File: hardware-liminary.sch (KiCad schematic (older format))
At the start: 51 parts, among them IC1 MCP6001T-I_OT, J1 Conn_01x05, J2 Conn_01x03, J3 Conn_01x03, J4 SWD, J5 Console, J6 UFL-Conn, K1 HL2-1CH-12S, Q1 CMBT3904, Q2 PT204-6C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

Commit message: relay
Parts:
- removed K1: HL2-1CH-12S, symbol Relay:DIPxx-1Cxx-51x
- added K?: HL2-1CH-12S, Relay_THT:HL2-1CH-12S, symbol proyect_new:HL2-1CH-12S
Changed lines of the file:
@@
 	850  3200 1050 3200
-$Comp
-L Relay:DIPxx-1Cxx-51x K1
-U 1 1 5F8071A4
-P 6200 7700
-F 0 "K1" V 6767 7700 50  0000 C CNN
-F 1 "HL2-1CH-12S" V 6676 7700 50  0000 C CNN
-F 2 "" H 6650 7650 50  0001 L CNN
-F 3 "https://standexelectronics.com/wp-content/uploads/datasheet_reed_relay_DIP.pdf" H 6200 7700 50  0001 C CNN
-	1    6200 7700
-	0    -1   -1   0
-$EndComp
 $Comp
 L Diode:1N4007 D1
@@
 Wire Wire Line
 	2600 1350 3000 1350
+$Comp
+L proyect_new:HL2-1CH-12S K?
+U 1 1 5F7D0ED4
+P 6200 7700
+F 0 "K?" V 6767 7700 50  0000 C CNN
+F 1 "HL2-1CH-12S" V 6676 7700 50  0000 C CNN
+F 2 "Relay_THT:HL2-1CH-12S" H 6650 7650 50  0001 L CNN
+F 3 "https://standexelectronics.com/wp-content/uploads/datasheet_reed_relay_DIP.pdf" H 6200 7700 50  0001 C CNN
+	1    6200 7700
+	0    -1   -1   0
+$EndComp
 $EndSCHEMATC

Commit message: Todas las footprint asignadas
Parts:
- removed L2: L_Core_Iron, symbol Device:L_Core_Iron
- added L2: L_Core_Ferrite, Inductor_SMD:L_0805_2012Metric_Pad1.15x1.40mm_HandSolder, symbol Device:L_Core_Ferrite
- JP2: footprint (none) -> Jumper:SolderJumper-2_P1.3mm_Open_TrianglePad1.0x1.5mm
- L1: footprint (none) -> Inductor_SMD:L_Taiyo-Yuden_MD-2020
- Q1, Q3, U2: footprint (none) -> Package_TO_SOT_SMD:SOT-23_Handsoldering
- SW1: footprint (none) -> Button_Switch_SMD:SW_Push_1P1T_NO_6x6mm_H9.5mm
- gave numbers to parts that had none: 1
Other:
- note added: "Program & Console"
- note removed: "Program & Debug"
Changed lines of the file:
@@
 F 0 "L1" V 7240 900 50  0000 C CNN
 F 1 "3.3uH" V 7149 900 50  0000 C CNN
-F 2 "" H 7050 900 50  0001 C CNN
+F 2 "Inductor_SMD:L_Taiyo-Yuden_MD-2020" H 7050 900 50  0001 C CNN
 F 3 "~" H 7050 900 50  0001 C CNN
 	1    7050 900
-	0    -1   -1   0
-$EndComp
-$Comp
-L Device:L_Core_Iron L2
-U 1 1 5F74052A
-P 6350 1950
-F 0 "L2" V 6575 1950 50  0000 C CNN
-F 1 "L_Core_Iron" V 6484 1950 50  0000 C CNN
-F 2 "" H 6350 1950 50  0001 C CNN
-F 3 "~" H 6350 1950 50  0001 C CNN
-	1    6350 1950
 	0    -1   -1   0
 $EndComp
@@
 F 0 "U2" H 5700 1142 50  0000 C CNN
 F 1 "LD1117S33TR_SOT223" H 5700 1051 50  0000 C CNN
-F 2 "" H 5700 1100 50  0001 C CNN
+F 2 "Package_TO_SOT_SMD:SOT-23_Handsoldering" H 5700 1100 50  0001 C CNN
 F 3 "http://www.st.com/st-web-ui/static/active/en/resource/technical/document/datasheet/CD00000544.pdf" H 5800 650 50  0001 C CNN
 	1    5700 900
@@
 F 0 "Q3" H 1791 4096 50  0000 L CNN
 F 1 "CMBT2222A" H 1791 4005 50  0000 L CNN
-F 2 "" H 1800 4150 50  0001 C CNN
+F 2 "Package_TO_SOT_SMD:SOT-23_Handsoldering" H 1800 4150 50  0001 C CNN
 F 3 "~" H 1600 4050 50  0001 C CNN
 	1    1600 4050
@@
 F 0 "Q1" H 6841 8546 50  0000 L CNN
 F 1 "CMBT3904" H 6841 8455 50  0000 L CNN
-F 2 "" H 6850 8600 50  0001 C CNN
+F 2 "Package_TO_SOT_SMD:SOT-23_Handsoldering" H 6850 8600 50  0001 C CNN
 F 3 "~" H 6650 8500 50  0001 C CNN
 	1    6650 8500
@@
 F 0 "JP2" H 7000 7735 50  0000 C CNN
 F 1 "Jumper_2_Open" H 7000 7644 50  0000 C CNN
-F 2 "" H 7000 7500 50  0001 C CNN
+F 2 "Jumper:SolderJumper-2_P1.3mm_Open_TrianglePad1.0x1.5mm" H 7000 7500 50  0001 C CNN
 F 3 "~" H 7000 7500 50  0001 C CNN
 	1    7000 7500
@@
 F 0 "SW1" H 4600 6535 50  0000 C CNN
 F 1 "SW_Push" H 4600 6444 50  0000 C CNN
-F 2 "" H 4600 6450 50  0001 C CNN
+F 2 "Button_Switch_SMD:SW_Push_1P1T_NO_6x6mm_H9.5mm" H 4600 6450 50  0001 C CNN
 F 3 "~" H 4600 6450 50  0001 C CNN
 	1    4600 6250
@@
 $EndComp
 Text Notes 1000 9150 0    118  ~ 24
-Program & Debug
-Wire Notes Line
-	950  8950 950  10700
-Wire Notes Line
-	950  10700 2650 10700
-Wire Notes Line
-	2650 10700 2650 8950
-Wire Notes Line
-	2650 8950 950  8950
+Program & Console
 Text Notes 5250 7050 0    118  ~ 24
 Relay Module
@@
 $EndComp
 $Comp
-L power:GNDA #PWR0114
-U 1 1 5F89AEDC
-P 9050 9950
-F 0 "#PWR0114" H 9050 9700 50  0001 C CNN
-F 1 "GNDA" H 9055 9777 50  0000 C CNN
-F 2 "" H 9050 9950 50  0001 C CNN
-F 3 "" H 9050 9950 50  0001 C CNN
-	1    9050 9950
-	1    0    0    -1
-$EndComp
-$Comp
-L power:PWR_FLAG #FLG0101
-U 1 1 5F89C39F
-P 9050 9950
-F 0 "#FLG0101" H 9050 10025 50  0001 C CNN
-F 1 "PWR_FLAG" H 9050 10123 50  0000 C CNN
-F 2 "" H 9050 9950 50  0001 C CNN
-F 3 "~" H 9050 9950 50  0001 C CNN
-	1    9050 9950
-	1    0    0    -1
-$EndComp
-$Comp
 L proyect_12-22_LEDs:12-22SURSYGC_S530-A2_TR8 LED1
 U 1 1 5F8A983B
@@
 	2600 1350 3000 1350
 $Comp
-L proyect_new:HL2-1CH-12S K?
+L proyect_new:HL2-1CH-12S K1
 U 1 1 5F7D0ED4
 P 6200 7700
-F 0 "K?" V 6767 7700 50  0000 C CNN
+F 0 "K1" V 6767 7700 50  0000 C CNN
 F 1 "HL2-1CH-12S" V 6676 7700 50  0000 C CNN
 F 2 "Relay_THT:HL2-1CH-12S" H 6650 7650 50  0001 L CNN
@@
 	0    -1   -1   0
 $EndComp
+Wire Notes Line
+	950  8950 950  10600
+Wire Notes Line
+	950  10600 2800 10600
+Wire Notes Line
+	2800 10600 2800 8950
+Wire Notes Line
+	2800 8950 950  8950
+$Comp
+L Device:L_Core_Ferrite L2
+U 1 1 5F7A5248
+P 6350 1950
+F 0 "L2" V 6575 1950 50  0000 C CNN
+F 1 "L_Core_Ferrite" V 6484 1950 50  0000 C CNN
+F 2 "Inductor_SMD:L_0805_2012Metric_Pad1.15x1.40mm_HandSolder" H 6350 1950 50  0001 C CNN
+F 3 "~" H 6350 1950 50  0001 C CNN
+	1    6350 1950
+	0    -1   -1   0
+$EndComp

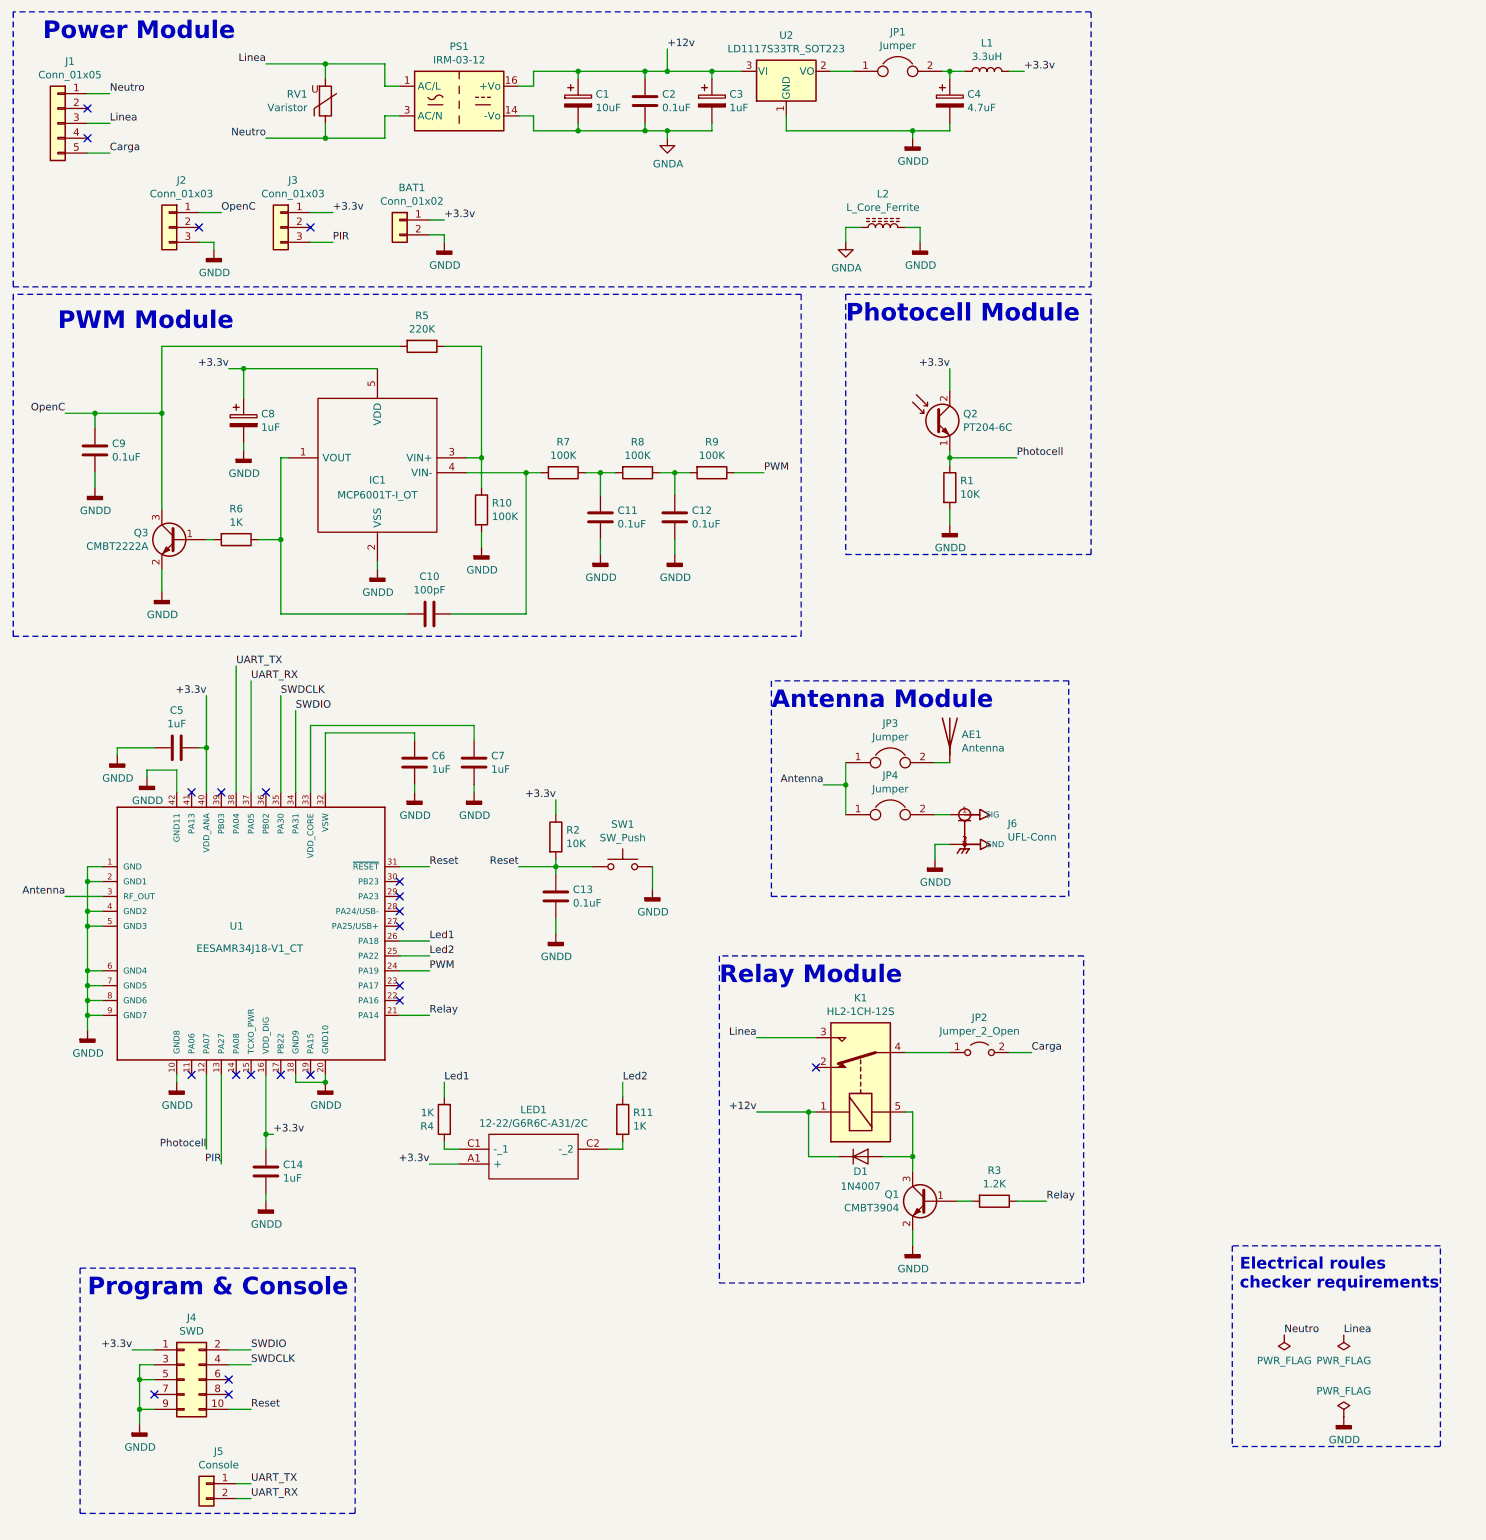
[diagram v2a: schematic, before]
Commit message: Esquematico separado en dos placas
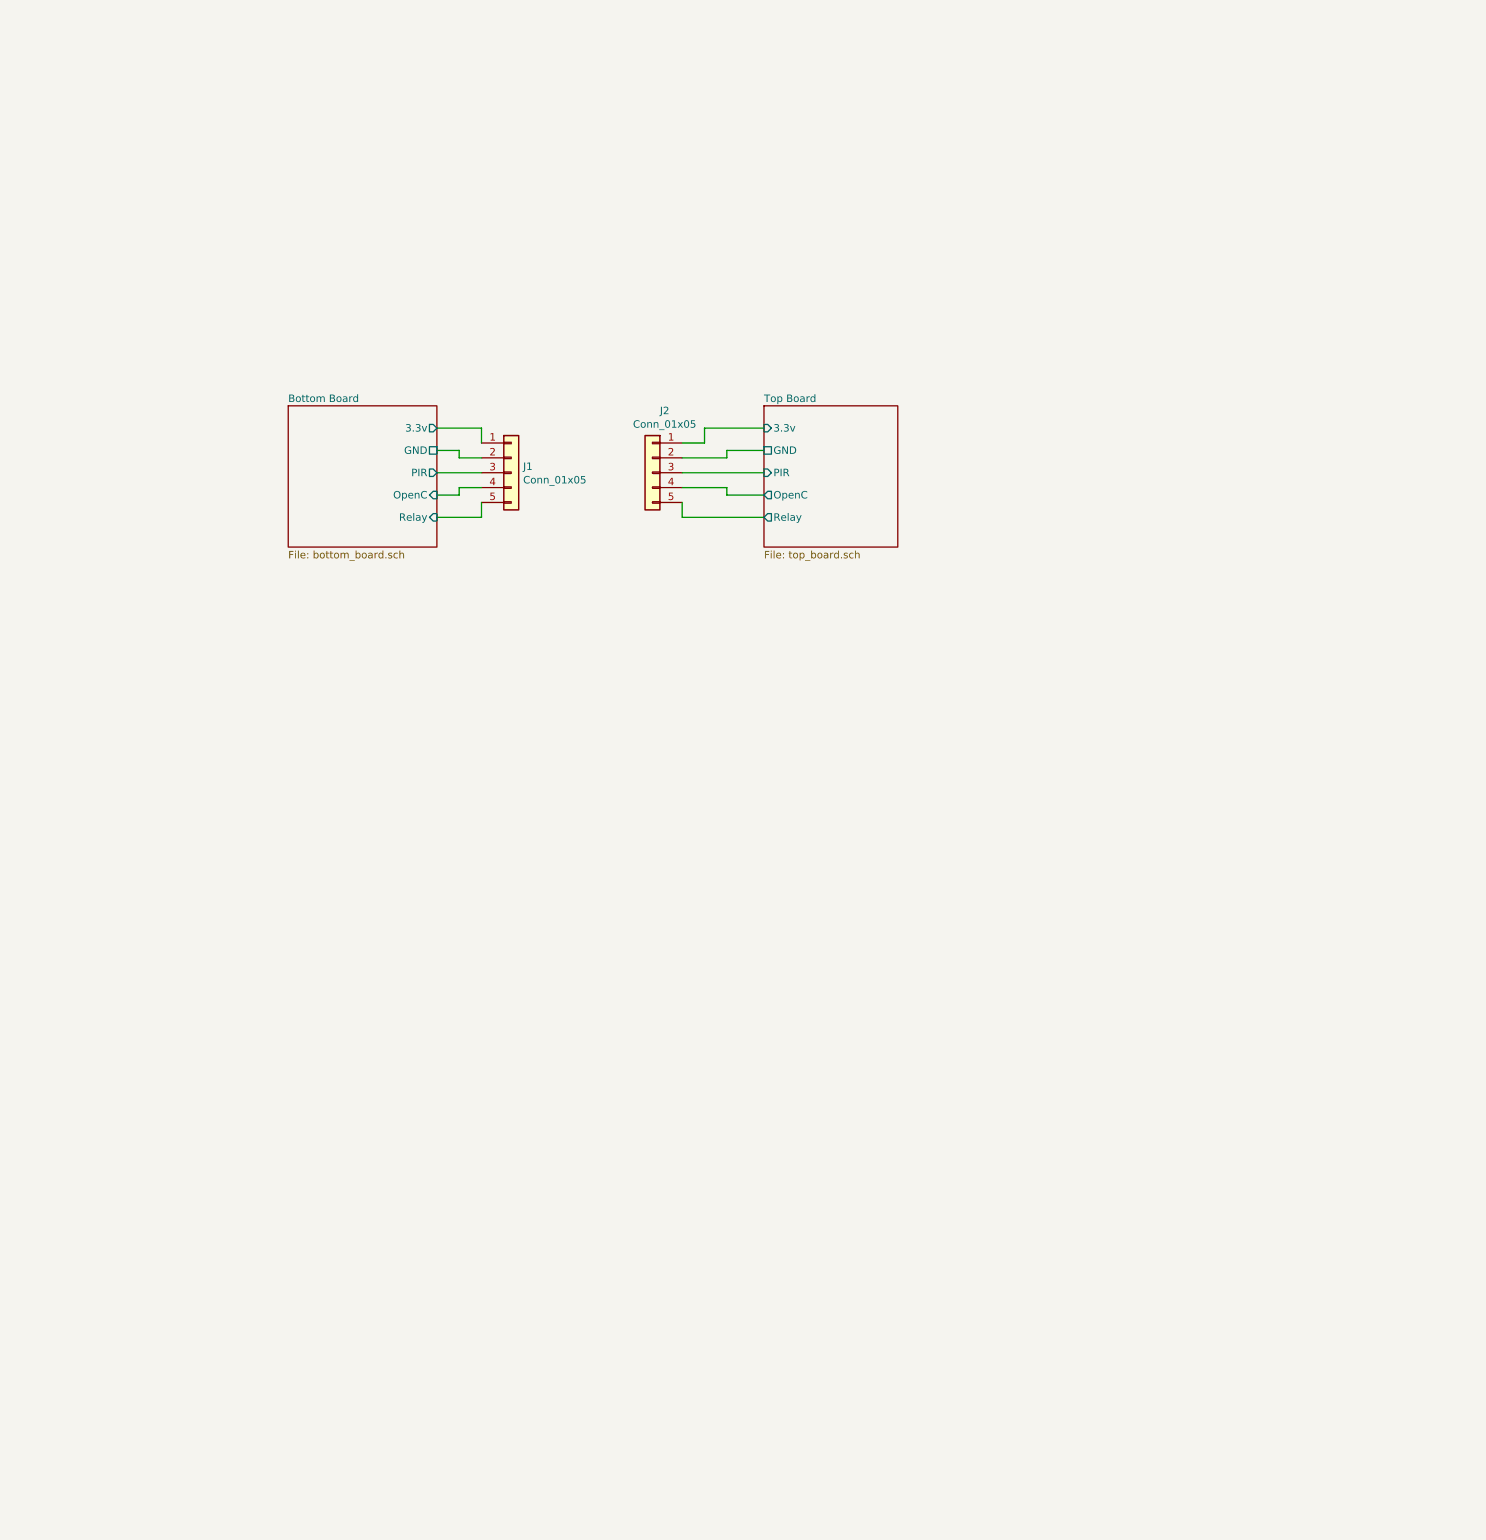
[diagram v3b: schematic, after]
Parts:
- removed AE1: Antenna, Connector_Pin:Pin_D1.3mm_L11.0mm_LooseFit, symbol Device:Antenna
- removed BAT1: Conn_01x02, Connector_PinHeader_2.54mm:PinHeader_1x02_P2.54mm_Vertical, symbol Connector_Generic:Conn_01x02
- removed C1: 10uF, Capacitor_THT:CP_Radial_D5.0mm_P2.00mm, symbol Device:CP
- removed C10: 100pF, Capacitor_SMD:C_1206_3216Metric_Pad1.42x1.75mm_HandSolder, symbol Device:C
- removed C11, C12, C13, C2, C9: 0.1uF, Capacitor_SMD:C_0805_2012Metric_Pad1.15x1.40mm_HandSolder, symbol Device:C
- removed C14, C5, C6, C7: 1uF, Capacitor_SMD:CP_Elec_4x5.3, symbol Device:C
- removed C3, C8: 1uF, Capacitor_SMD:CP_Elec_4x5.3, symbol Device:CP
- removed C4: 4.7uF, Capacitor_SMD:CP_Elec_4x5.4, symbol Device:CP
- removed D1: 1N4007, Diode_THT:D_DO-41_SOD81_P10.16mm_Horizontal, symbol Diode:1N4007
- removed IC1: MCP6001T-I_OT, proyect_MCP6001T-I_OT:SOT95P270X145-5N, symbol proyect_MCP6001T-I_OT:MCP6001T-I_OT
- removed J2, J3: Conn_01x03, Connector_PinHeader_2.54mm:PinHeader_1x03_P2.54mm_Vertical, symbol Connector_Generic:Conn_01x03
- removed J4: SWD, Connector_PinHeader_1.27mm:PinHeader_2x05_P1.27mm_Vertical, symbol Connector_Generic:Conn_02x05_Odd_Even
- removed J5: Console, Connector_PinHeader_2.54mm:PinHeader_1x02_P2.54mm_Vertical, symbol Connector_Generic:Conn_01x02
- removed J6: UFL-Conn, proyect_UFL-Conn:TE_1909763-1, symbol proyect_UFL-Conn:1909763-1
- removed JP1: Jumper, Connector_PinHeader_2.54mm:PinHeader_1x02_P2.54mm_Vertical, symbol Device:Jumper
- removed JP2: Jumper_2_Open, Jumper:SolderJumper-2_P1.3mm_Open_TrianglePad1.0x1.5mm, symbol Jumper:Jumper_2_Open
- removed JP3, JP4: Jumper, Resistor_SMD:R_1206_3216Metric_Pad1.42x1.75mm_HandSolder, symbol Device:Jumper
- removed K1: HL2-1CH-12S, Relay_THT:HL2-1CH-12S, symbol proyect_new:HL2-1CH-12S
- removed L1: 3.3uH, Inductor_SMD:L_Taiyo-Yuden_MD-2020, symbol Device:L
- removed L2: L_Core_Ferrite, Inductor_SMD:L_0805_2012Metric_Pad1.15x1.40mm_HandSolder, symbol Device:L_Core_Ferrite
- removed LED1: 12-22/G6R6C-A31/2C, proyect_12-22_LEDs:1222SURSYGCS530A2TR8, symbol proyect_12-22_LEDs:12-22SURSYGC_S530-A2_TR8
- removed PS1: IRM-03-12, proyect_new:Converter_ACDC_MeanWell_IRM-03-xx_THT, symbol Converter_ACDC:IRM-03-12
- removed Q1: CMBT3904, Package_TO_SOT_SMD:SOT-23_Handsoldering, symbol Device:Q_NPN_BEC
- removed Q2: PT204-6C, LED_THT:LED_D5.0mm_Clear, symbol Device:Q_Photo_NPN_EC
- removed Q3: CMBT2222A, Package_TO_SOT_SMD:SOT-23_Handsoldering, symbol Device:Q_NPN_BEC
- removed R1, R2: 10K, Resistor_SMD:R_1206_3216Metric_Pad1.42x1.75mm_HandSolder, symbol Device:R
- removed R10, R7, R8, R9: 100K, Resistor_SMD:R_1206_3216Metric_Pad1.42x1.75mm_HandSolder, symbol Device:R
- removed R11, R4, R6: 1K, Resistor_SMD:R_1206_3216Metric_Pad1.42x1.75mm_HandSolder, symbol Device:R
- removed R3: 1.2K, Resistor_SMD:R_1206_3216Metric_Pad1.42x1.75mm_HandSolder, symbol Device:R
- removed R5: 220K, Resistor_SMD:R_1206_3216Metric_Pad1.42x1.75mm_HandSolder, symbol Device:R
- removed RV1: Varistor, Varistor:RV_Disc_D15.5mm_W3.9mm_P7.5mm, symbol Device:Varistor
- removed SW1: SW_Push, Button_Switch_SMD:SW_Push_1P1T_NO_6x6mm_H9.5mm, symbol Switch:SW_Push
- removed U1: EESAMR34J18-V1_CT, proyect_EESAMR34:EESAMR34, symbol proyect_EESAMR34J18-V1_CT:EESAMR34J18-V1_CT
- removed U2: LD1117S33TR_SOT223, Package_TO_SOT_SMD:SOT-23_Handsoldering, symbol Regulator_Linear:LD1117S33TR_SOT223
- added J2: Conn_01x05, Connector_PinHeader_2.54mm:PinHeader_1x05_P2.54mm_Vertical, symbol Connector_Generic:Conn_01x05
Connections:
- net Bottom Board/GND: now reaches J1.2 (Pin_2)
- net Bottom Board/OpenC: now reaches J1.4 (Pin_4)
- net Carga renamed Bottom Board/Relay
- net Linea renamed Bottom Board/PIR
- net Neutro renamed Bottom Board/3.3v
- new net Top Board/3.3v: J2.1 (Pin_1)
- new net Top Board/GND: J2.2 (Pin_2)
- new net Top Board/OpenC: J2.4 (Pin_4)
- new net Top Board/PIR: J2.3 (Pin_3)
- new net Top Board/Relay: J2.5 (Pin_5)
- no-connect marks 22 -> 0
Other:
- note removed: "Antenna Module"
- note removed: "Electrical roules \nchecker requirements"
- note removed: "PWM Module"
- note removed: "Photocell Module"
- note removed: "Power Module"
- note removed: "Program & Console"
- note removed: "Relay Module"
